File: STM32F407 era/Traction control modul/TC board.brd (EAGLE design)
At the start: 69.8 x 100 mm, 18 parts, among them IC1 74HC14D, IC2 lm2575, U1 MAX13052ESA+

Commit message: merged TC board with AUX board
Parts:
- added J2: (no value), unicorn_v2:AUTOCONNECTOR
- moved C2 62.4 mm to (-46.4, 32.4)
- moved IC2 62.4 mm to (-41.3, 17.8)
- moved L1 62.4 mm to (-43.2, 43.2)
- moved R1 62.4 mm to (-43.2, 26.7)
- moved C1 62.4 mm to (-37.5, 32.4)
- moved R2 62.4 mm to (-44.5, 26.7)
- moved D1 62.4 mm to (-41.9, 51.4)
- moved H2 50.8 mm to (-46.4, 95.9)
- moved H3 50.8 mm to (-46.4, 4.45)
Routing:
- net 12V: track 57.8 -> 11.6 mm
- net 3.3V: track 195.7 -> 210.3 mm
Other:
- board size 69.8 x 100 mm -> 120.6 x 100 mm
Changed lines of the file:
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@@
 <board>
 <plain>
-<wire x1="0" y1="0" x2="69.83" y2="0" width="0" layer="20"/>
+<wire x1="-50.8" y1="0" x2="69.83" y2="0" width="0" layer="20"/>
 <wire x1="69.83" y1="0" x2="69.83" y2="100" width="0" layer="20"/>
-<wire x1="69.83" y1="100" x2="0" y2="100" width="0" layer="20"/>
-<wire x1="0" y1="100" x2="0" y2="0" width="0" layer="20"/>
+<wire x1="69.83" y1="100" x2="-50.8" y2="100" width="0" layer="20"/>
+<wire x1="-50.8" y1="100" x2="-50.8" y2="0" width="0" layer="20"/>
 </plain>
 <attributes>
@@
 <element name="IC1" library="74xx-eu" package="SO14" value="74HC14D" x="62.23" y="59.69" rot="R90"/>
 <element name="H1" library="holes" package="3,0" value="MOUNT-HOLE3.0" x="66.04" y="95.885"/>
-<element name="H2" library="holes" package="3,0" value="MOUNT-HOLE3.0" x="4.445" y="95.885"/>
-<element name="H3" library="holes" package="3,0" value="MOUNT-HOLE3.0" x="4.445" y="4.445"/>
+<element name="H2" library="holes" package="3,0" value="MOUNT-HOLE3.0" x="-46.355" y="95.885"/>
+<element name="H3" library="holes" package="3,0" value="MOUNT-HOLE3.0" x="-46.355" y="4.445"/>
 <element name="H4" library="holes" package="3,0" value="MOUNT-HOLE3.0" x="66.04" y="4.445"/>
-<element name="IC2" library="linear" package="TO263-5" value="lm2575" x="9.525" y="53.975" rot="R180"/>
-<element name="C1" library="rcl" package="E2,5-7" value="100u" x="13.335" y="68.58" rot="R90"/>
-<element name="R1" library="microbuilder" package="_0603" value="1k" x="7.62" y="62.865" rot="R270"/>
-<element name="R2" library="microbuilder" package="_0603" value="1k69" x="6.35" y="62.865" rot="R270"/>
-<element name="L1" library="SparkFun-Passives" package="CDRH125" value="MSS1278-224KLD" x="7.62" y="79.375" rot="R270"/>
-<element name="D1" library="diode" package="F126Z12" value="1n5824" x="8.89" y="87.63" rot="R180"/>
-<element name="C2" library="rcl" package="E3,5-8" value="220uf" x="4.445" y="68.58" rot="R180"/>
+<element name="IC2" library="linear" package="TO263-5" value="lm2575" x="-41.275" y="17.78" rot="R180"/>
+<element name="C1" library="rcl" package="E2,5-7" value="100u" x="-37.465" y="32.385" rot="R90"/>
+<element name="R1" library="microbuilder" package="_0603" value="1k" x="-43.18" y="26.67" rot="R270"/>
+<element name="R2" library="microbuilder" package="_0603" value="1k69" x="-44.45" y="26.67" rot="R270"/>
+<element name="L1" library="SparkFun-Passives" package="CDRH125" value="MSS1278-224KLD" x="-43.18" y="43.18" rot="R270"/>
+<element name="D1" library="diode" package="F126Z12" value="1n5824" x="-41.91" y="51.435" rot="R180"/>
+<element name="C2" library="rcl" package="E3,5-8" value="220uf" x="-46.355" y="32.385" rot="R180"/>
 <element name="C3" library="microbuilder" package="_0603" value="100n" x="55.88" y="55.88" rot="R180"/>
 <element name="U1" library="Maxim_By_element14_Batch_1" package="SOIC127P600X175-8N" value="MAX13052ESA+" x="49.53" y="18.415" rot="R90">
@@
 <element name="R3" library="microbuilder" package="_0603" value="1k8" x="49.53" y="23.495"/>
 <element name="C4" library="microbuilder" package="_0603" value="100n" x="45.72" y="18.415" rot="R90"/>
+<element name="J2" library="unicorn_v2" package="AUTOCONNECTOR" value="" x="-13.97" y="74.93"/>
 </elements>
 <signals>
 <signal name="GND">
 <polygon width="0.4064" layer="16">
-<vertex x="0" y="0"/>
+<vertex x="-50.8" y="0"/>
 <vertex x="69.85" y="0"/>
 <vertex x="69.85" y="100.33"/>
-<vertex x="0" y="100.33"/>
+<vertex x="-50.8" y="100.33"/>
 </polygon>
 <polygon width="0.4064" layer="1">
-<vertex x="0" y="0"/>
+<vertex x="-50.8" y="0"/>
 <vertex x="69.85" y="0"/>
 <vertex x="69.85" y="100.33"/>
-<vertex x="0" y="100.33"/>
+<vertex x="-50.8" y="100.33"/>
 </polygon>
 <contactref element="U$1" pad="P$21"/>
@@
 <contactref element="L1" pad="2"/>
 <contactref element="C2" pad="+"/>
-<wire x1="2.72" y1="79.375" x2="2.72" y2="72.083" width="1.016" layer="1"/>
-<wire x1="2.72" y1="72.083" x2="6.223" y2="68.58" width="1.016" layer="1"/>
-<wire x1="6.223" y1="68.58" x2="6.223" y2="27.432" width="0.4064" layer="16"/>
-<wire x1="6.223" y1="27.432" x2="13.43025" y2="20.22475" width="0.4064" layer="16"/>
-<wire x1="13.43025" y1="20.22475" x2="19.46275" y2="20.22475" width="0.4064" layer="16"/>
-<wire x1="6.35" y1="63.627" x2="6.223" y2="63.627" width="0.4064" layer="1"/>
-<wire x1="6.223" y1="63.627" x2="6.223" y2="68.58" width="0.4064" layer="1"/>
+<wire x1="-48.08" y1="43.18" x2="-48.08" y2="35.888" width="1.016" layer="1"/>
+<wire x1="-48.08" y1="35.888" x2="-44.577" y2="32.385" width="1.016" layer="1"/>
+<wire x1="-44.577" y1="32.385" x2="-44.577" y2="27.432" width="0.4064" layer="16"/>
+<wire x1="-44.577" y1="27.432" x2="-37.36975" y2="20.22475" width="0.4064" layer="16"/>
+<wire x1="-37.36975" y1="20.22475" x2="19.46275" y2="20.22475" width="0.4064" layer="16"/>
+<wire x1="-44.45" y1="27.432" x2="-44.577" y2="27.432" width="0.4064" layer="1"/>
+<wire x1="-44.577" y1="27.432" x2="-44.577" y2="32.385" width="0.4064" layer="1"/>
 <contactref element="IC1" pad="14"/>
 <contactref element="C3" pad="1"/>
@@
 <contactref element="J1" pad="M1"/>
 <contactref element="C1" pad="+"/>
-<wire x1="24.89" y1="68.01" x2="17.145" y2="68.01" width="1.27" layer="1"/>
-<wire x1="17.145" y1="68.01" x2="14.035" y2="68.01" width="1.27" layer="1"/>
-<wire x1="14.035" y1="68.01" x2="13.335" y2="67.31" width="1.27" layer="1"/>
-<wire x1="13.335" y1="67.31" x2="12.9286" y2="66.9036" width="1.27" layer="1"/>
-<wire x1="12.9286" y1="66.9036" x2="12.9286" y2="59.7662" width="1.27" layer="1"/>
+<wire x1="-36.765" y1="31.815" x2="-37.465" y2="31.115" width="1.27" layer="1"/>
+<wire x1="-37.465" y1="31.115" x2="-37.8714" y2="30.7086" width="1.27" layer="1"/>
+<wire x1="-37.8714" y1="30.7086" x2="-37.8714" y2="23.5712" width="1.27" layer="1"/>
 <contactref element="J1" pad="G4"/>
 <wire x1="39.59" y1="80.01" x2="39.59" y2="81.695" width="0.6096" layer="1"/>
 <wire x1="39.59" y1="81.695" x2="38.735" y2="82.55" width="0.6096" layer="1"/>
-<wire x1="38.735" y1="82.55" x2="18.415" y2="82.55" width="0.6096" layer="1"/>
-<wire x1="18.415" y1="82.55" x2="17.145" y2="81.28" width="0.6096" layer="1"/>
-<wire x1="17.145" y1="81.28" x2="17.145" y2="68.01" width="0.6096" layer="1"/>
+<wire x1="24.89" y1="68.01" x2="39.59" y2="80.01" width="0" layer="19" extent="1-1"/>
+<wire x1="-36.765" y1="31.815" x2="24.89" y2="68.01" width="0" layer="19" extent="1-1"/>
 </signal>
 <signal name="N$1">
@@
 <contactref element="R1" pad="2"/>
 <contactref element="R2" pad="2"/>
-<wire x1="7.8232" y1="59.7662" x2="7.62" y2="59.7662" width="0.4064" layer="1"/>
-<wire x1="7.62" y1="59.7662" x2="7.62" y2="62.103" width="0.4064" layer="1"/>
-<wire x1="7.62" y1="62.103" x2="6.35" y2="62.103" width="0.4064" layer="1"/>
+<wire x1="-42.9768" y1="23.5712" x2="-43.18" y2="23.5712" width="0.4064" layer="1"/>
+<wire x1="-43.18" y1="23.5712" x2="-43.18" y2="25.908" width="0.4064" layer="1"/>
+<wire x1="-43.18" y1="25.908" x2="-44.45" y2="25.908" width="0.4064" layer="1"/>
 </signal>
 <signal name="N$2">
@@
 <contactref element="L1" pad="1"/>
 <contactref element="D1" pad="C"/>
-<wire x1="11.2268" y1="59.7662" x2="11.2268" y2="77.4468" width="1.016" layer="1"/>
-<wire x1="11.2268" y1="77.4468" x2="12.52" y2="79.375" width="1.016" layer="1"/>
-<wire x1="12.52" y1="79.375" x2="12.52" y2="86.815" width="1.016" layer="1"/>
-<wire x1="12.52" y1="86.815" x2="13.335" y2="87.63" width="1.016" layer="1"/>
-<wire x1="13.335" y1="87.63" x2="15.24" y2="87.63" width="1.016" layer="1"/>
+<wire x1="-39.5732" y1="23.5712" x2="-39.5732" y2="41.2518" width="1.016" layer="1"/>
+<wire x1="-39.5732" y1="41.2518" x2="-38.28" y2="43.18" width="1.016" layer="1"/>
+<wire x1="-38.28" y1="43.18" x2="-38.28" y2="50.62" width="1.016" layer="1"/>
+<wire x1="-38.28" y1="50.62" x2="-37.465" y2="51.435" width="1.016" layer="1"/>
+<wire x1="-37.465" y1="51.435" x2="-35.56" y2="51.435" width="1.016" layer="1"/>
 </signal>
 <signal name="N$3">
@@
 <wire x1="44.45" y1="59.69" x2="43.18" y2="60.96" width="0.4064" layer="1"/>
 <via x="43.18" y="60.96" extent="1-16" drill="0.5" shape="octagon"/>
-<wire x1="43.18" y1="60.96" x2="42.545" y2="61.595" width="0.4064" layer="16"/>
-<wire x1="42.545" y1="61.595" x2="42.545" y2="62.865" width="0.4064" layer="16"/>
-<wire x1="42.545" y1="62.865" x2="41.91" y2="63.5" width="0.4064" layer="16"/>
-<wire x1="41.91" y1="63.5" x2="41.91" y2="64.135" width="0.4064" layer="16"/>
+<wire x1="43.18" y1="60.96" x2="41.91" y2="62.23" width="0.4064" layer="16"/>
+<wire x1="41.91" y1="62.23" x2="41.91" y2="64.135" width="0.4064" layer="16"/>
 <wire x1="41.91" y1="64.135" x2="43.33875" y2="65.56375" width="0.4064" layer="16"/>
 <wire x1="43.33875" y1="65.56375" x2="43.33875" y2="74.76125" width="0.4064" layer="16"/>

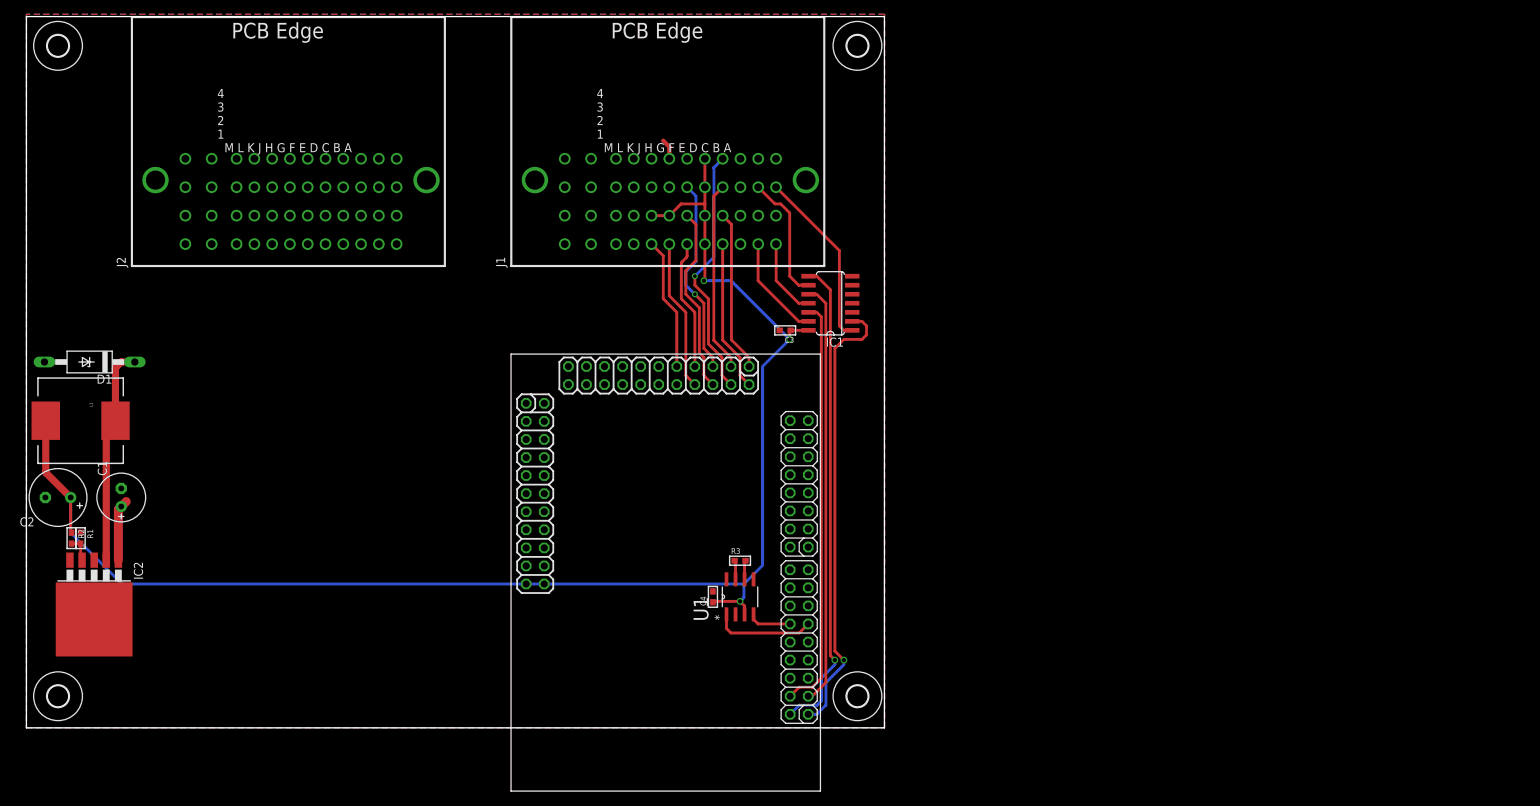
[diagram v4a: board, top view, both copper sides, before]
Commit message: fixed CAN controller connections
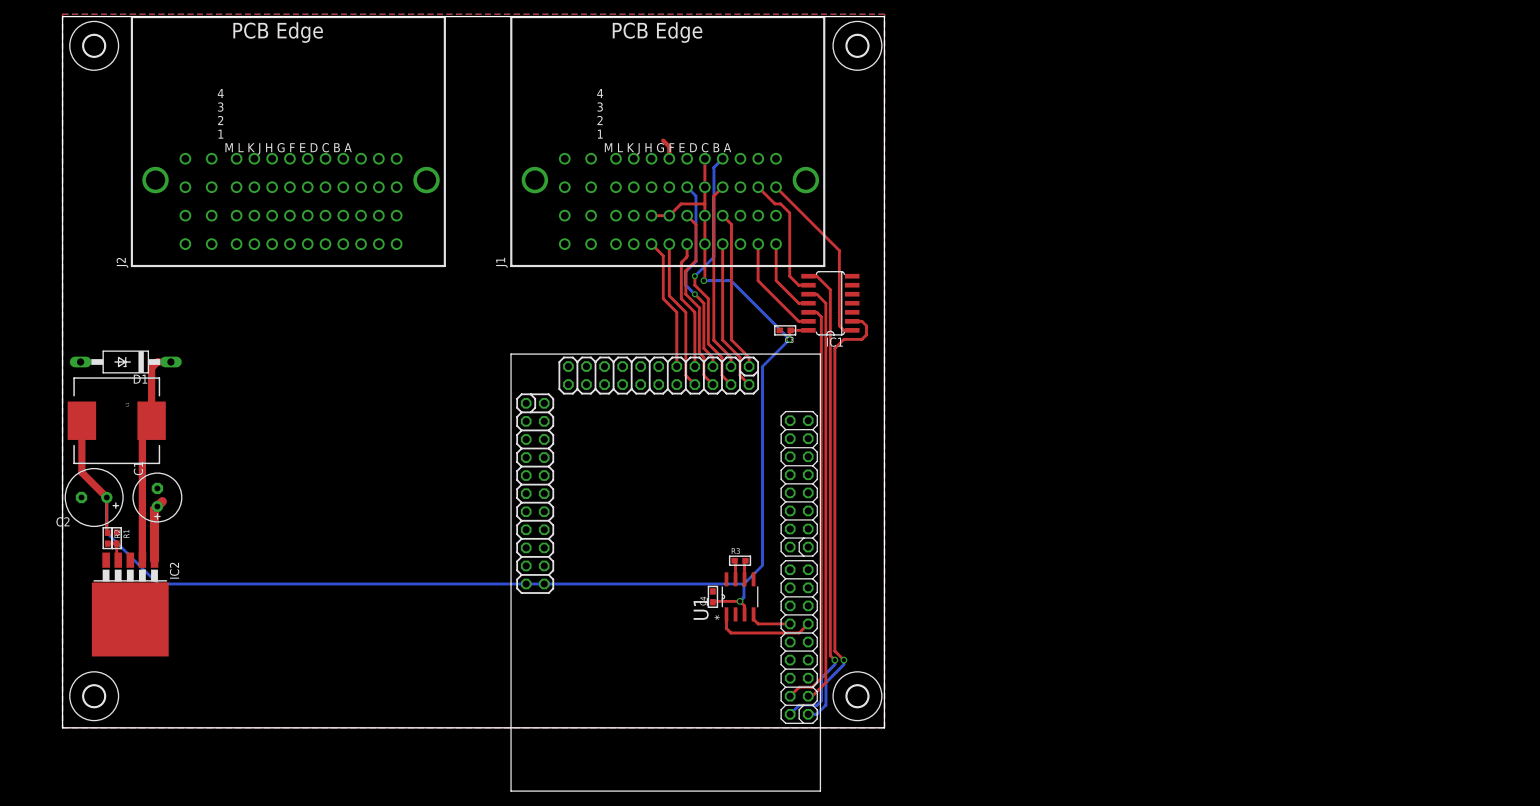
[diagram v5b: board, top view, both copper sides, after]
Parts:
- moved C1 5.08 mm to (-32.4, 32.4)
- moved R2 5.08 mm to (-39.4, 26.7)
- moved C2 5.08 mm to (-41.3, 32.4)
- moved D1 5.08 mm to (-36.8, 51.4)
- moved H2 5.08 mm to (-41.3, 95.9)
- moved H3 5.08 mm to (-41.3, 4.45)
- moved IC2 5.08 mm to (-36.2, 17.8)
- moved L1 5.08 mm to (-38.1, 43.2)
- moved R1 5.08 mm to (-38.1, 26.7)
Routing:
- net 3.3V: track 210.3 -> 205.2 mm
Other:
- board size 120.6 x 100 mm -> 115.5 x 100 mm
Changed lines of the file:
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@@
 <board>
 <plain>
-<wire x1="-50.8" y1="0" x2="69.83" y2="0" width="0" layer="20"/>
+<wire x1="-45.72" y1="0" x2="69.83" y2="0" width="0" layer="20"/>
 <wire x1="69.83" y1="0" x2="69.83" y2="100" width="0" layer="20"/>
-<wire x1="69.83" y1="100" x2="-50.8" y2="100" width="0" layer="20"/>
-<wire x1="-50.8" y1="100" x2="-50.8" y2="0" width="0" layer="20"/>
+<wire x1="69.83" y1="100" x2="-45.72" y2="100" width="0" layer="20"/>
+<wire x1="-45.72" y1="100" x2="-45.72" y2="0" width="0" layer="20"/>
 </plain>
 <attributes>
@@
 <element name="IC1" library="74xx-eu" package="SO14" value="74HC14D" x="62.23" y="59.69" rot="R90"/>
 <element name="H1" library="holes" package="3,0" value="MOUNT-HOLE3.0" x="66.04" y="95.885"/>
-<element name="H2" library="holes" package="3,0" value="MOUNT-HOLE3.0" x="-46.355" y="95.885"/>
-<element name="H3" library="holes" package="3,0" value="MOUNT-HOLE3.0" x="-46.355" y="4.445"/>
+<element name="H2" library="holes" package="3,0" value="MOUNT-HOLE3.0" x="-41.275" y="95.885"/>
+<element name="H3" library="holes" package="3,0" value="MOUNT-HOLE3.0" x="-41.275" y="4.445"/>
 <element name="H4" library="holes" package="3,0" value="MOUNT-HOLE3.0" x="66.04" y="4.445"/>
-<element name="IC2" library="linear" package="TO263-5" value="lm2575" x="-41.275" y="17.78" rot="R180"/>
-<element name="C1" library="rcl" package="E2,5-7" value="100u" x="-37.465" y="32.385" rot="R90"/>
-<element name="R1" library="microbuilder" package="_0603" value="1k" x="-43.18" y="26.67" rot="R270"/>
-<element name="R2" library="microbuilder" package="_0603" value="1k69" x="-44.45" y="26.67" rot="R270"/>
-<element name="L1" library="SparkFun-Passives" package="CDRH125" value="MSS1278-224KLD" x="-43.18" y="43.18" rot="R270"/>
-<element name="D1" library="diode" package="F126Z12" value="1n5824" x="-41.91" y="51.435" rot="R180"/>
-<element name="C2" library="rcl" package="E3,5-8" value="220uf" x="-46.355" y="32.385" rot="R180"/>
+<element name="IC2" library="linear" package="TO263-5" value="lm2575" x="-36.195" y="17.78" rot="R180"/>
+<element name="C1" library="rcl" package="E2,5-7" value="100u" x="-32.385" y="32.385" rot="R90"/>
+<element name="R1" library="microbuilder" package="_0603" value="1k" x="-38.1" y="26.67" rot="R270"/>
+<element name="R2" library="microbuilder" package="_0603" value="1k69" x="-39.37" y="26.67" rot="R270"/>
+<element name="L1" library="SparkFun-Passives" package="CDRH125" value="MSS1278-224KLD" x="-38.1" y="43.18" rot="R270"/>
+<element name="D1" library="diode" package="F126Z12" value="1n5824" x="-36.83" y="51.435" rot="R180"/>
+<element name="C2" library="rcl" package="E3,5-8" value="220uf" x="-41.275" y="32.385" rot="R180"/>
 <element name="C3" library="microbuilder" package="_0603" value="100n" x="55.88" y="55.88" rot="R180"/>
 <element name="U1" library="Maxim_By_element14_Batch_1" package="SOIC127P600X175-8N" value="MAX13052ESA+" x="49.53" y="18.415" rot="R90">
@@
 <signal name="GND">
 <polygon width="0.4064" layer="16">
-<vertex x="-50.8" y="0"/>
+<vertex x="-45.72" y="0"/>
 <vertex x="69.85" y="0"/>
 <vertex x="69.85" y="100.33"/>
-<vertex x="-50.8" y="100.33"/>
+<vertex x="-45.72" y="100.33"/>
 </polygon>
 <polygon width="0.4064" layer="1">
-<vertex x="-50.8" y="0"/>
+<vertex x="-45.72" y="0"/>
 <vertex x="69.85" y="0"/>
 <vertex x="69.85" y="100.33"/>
-<vertex x="-50.8" y="100.33"/>
+<vertex x="-45.72" y="100.33"/>
 </polygon>
 <contactref element="U$1" pad="P$21"/>
@@
 <contactref element="L1" pad="2"/>
 <contactref element="C2" pad="+"/>
-<wire x1="-48.08" y1="43.18" x2="-48.08" y2="35.888" width="1.016" layer="1"/>
-<wire x1="-48.08" y1="35.888" x2="-44.577" y2="32.385" width="1.016" layer="1"/>
-<wire x1="-44.577" y1="32.385" x2="-44.577" y2="27.432" width="0.4064" layer="16"/>
-<wire x1="-44.577" y1="27.432" x2="-37.36975" y2="20.22475" width="0.4064" layer="16"/>
-<wire x1="-37.36975" y1="20.22475" x2="19.46275" y2="20.22475" width="0.4064" layer="16"/>
-<wire x1="-44.45" y1="27.432" x2="-44.577" y2="27.432" width="0.4064" layer="1"/>
-<wire x1="-44.577" y1="27.432" x2="-44.577" y2="32.385" width="0.4064" layer="1"/>
+<wire x1="-43" y1="43.18" x2="-43" y2="35.888" width="1.016" layer="1"/>
+<wire x1="-43" y1="35.888" x2="-39.497" y2="32.385" width="1.016" layer="1"/>
+<wire x1="-39.497" y1="32.385" x2="-39.497" y2="27.432" width="0.4064" layer="16"/>
+<wire x1="-39.497" y1="27.432" x2="-32.28975" y2="20.22475" width="0.4064" layer="16"/>
+<wire x1="-32.28975" y1="20.22475" x2="19.46275" y2="20.22475" width="0.4064" layer="16"/>
+<wire x1="-39.37" y1="27.432" x2="-39.497" y2="27.432" width="0.4064" layer="1"/>
+<wire x1="-39.497" y1="27.432" x2="-39.497" y2="32.385" width="0.4064" layer="1"/>
 <contactref element="IC1" pad="14"/>
 <contactref element="C3" pad="1"/>
@@
 <contactref element="J1" pad="M1"/>
 <contactref element="C1" pad="+"/>
-<wire x1="-36.765" y1="31.815" x2="-37.465" y2="31.115" width="1.27" layer="1"/>
-<wire x1="-37.465" y1="31.115" x2="-37.8714" y2="30.7086" width="1.27" layer="1"/>
-<wire x1="-37.8714" y1="30.7086" x2="-37.8714" y2="23.5712" width="1.27" layer="1"/>
+<wire x1="-31.685" y1="31.815" x2="-32.385" y2="31.115" width="1.27" layer="1"/>
+<wire x1="-32.385" y1="31.115" x2="-32.7914" y2="30.7086" width="1.27" layer="1"/>
+<wire x1="-32.7914" y1="30.7086" x2="-32.7914" y2="23.5712" width="1.27" layer="1"/>
 <contactref element="J1" pad="G4"/>
 <wire x1="39.59" y1="80.01" x2="39.59" y2="81.695" width="0.6096" layer="1"/>
 <wire x1="39.59" y1="81.695" x2="38.735" y2="82.55" width="0.6096" layer="1"/>
 <wire x1="24.89" y1="68.01" x2="39.59" y2="80.01" width="0" layer="19" extent="1-1"/>
-<wire x1="-36.765" y1="31.815" x2="24.89" y2="68.01" width="0" layer="19" extent="1-1"/>
+<wire x1="-31.685" y1="31.815" x2="24.89" y2="68.01" width="0" layer="19" extent="1-1"/>
 </signal>
 <signal name="N$1">
@@
 <contactref element="R1" pad="2"/>
 <contactref element="R2" pad="2"/>
-<wire x1="-42.9768" y1="23.5712" x2="-43.18" y2="23.5712" width="0.4064" layer="1"/>
-<wire x1="-43.18" y1="23.5712" x2="-43.18" y2="25.908" width="0.4064" layer="1"/>
-<wire x1="-43.18" y1="25.908" x2="-44.45" y2="25.908" width="0.4064" layer="1"/>
+<wire x1="-37.8968" y1="23.5712" x2="-38.1" y2="23.5712" width="0.4064" layer="1"/>
+<wire x1="-38.1" y1="23.5712" x2="-38.1" y2="25.908" width="0.4064" layer="1"/>
+<wire x1="-38.1" y1="25.908" x2="-39.37" y2="25.908" width="0.4064" layer="1"/>
 </signal>
 <signal name="N$2">
@@
 <contactref element="L1" pad="1"/>
 <contactref element="D1" pad="C"/>
-<wire x1="-39.5732" y1="23.5712" x2="-39.5732" y2="41.2518" width="1.016" layer="1"/>
-<wire x1="-39.5732" y1="41.2518" x2="-38.28" y2="43.18" width="1.016" layer="1"/>
-<wire x1="-38.28" y1="43.18" x2="-38.28" y2="50.62" width="1.016" layer="1"/>
-<wire x1="-38.28" y1="50.62" x2="-37.465" y2="51.435" width="1.016" layer="1"/>
-<wire x1="-37.465" y1="51.435" x2="-35.56" y2="51.435" width="1.016" layer="1"/>
+<wire x1="-34.4932" y1="23.5712" x2="-34.4932" y2="41.2518" width="1.016" layer="1"/>
+<wire x1="-34.4932" y1="41.2518" x2="-33.2" y2="43.18" width="1.016" layer="1"/>
+<wire x1="-33.2" y1="43.18" x2="-33.2" y2="50.62" width="1.016" layer="1"/>
+<wire x1="-33.2" y1="50.62" x2="-32.385" y2="51.435" width="1.016" layer="1"/>
+<wire x1="-32.385" y1="51.435" x2="-30.48" y2="51.435" width="1.016" layer="1"/>
 </signal>
 <signal name="N$3">
